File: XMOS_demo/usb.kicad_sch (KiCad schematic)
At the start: 9 parts, among them J2 USB_C_Receptacle_USB2.0_16P, U4 TPD3S014

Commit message: sch work
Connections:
- net P5V0: now also U4.4 (OUT)
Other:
- company: (none) -> AGH University
- title: (none) -> USB Sound Card USB Port
- moved on the sheet: C22, C25, FB2, R17, U4

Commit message: Lots of sch work
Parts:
- C22, C23, C25: Max Voltage 10V -> 16V
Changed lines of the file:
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@@
 			)
 		)
-		(property "Max Voltage" "10V"
+		(property "Max Voltage" "16V"
 			(at 180.34 81.28 0)
 			(effects
@@
 			)
 		)
-		(property "Max Voltage" "10V"
+		(property "Max Voltage" "16V"
 			(at 152.4 81.28 0)
 			(effects
@@
 			)
 		)
-		(property "Max Voltage" "10V"
+		(property "Max Voltage" "16V"
 			(at 170.18 81.28 0)
 			(effects

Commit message: sch work, pcb import and initial board outline
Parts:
- added H5: VBUS, MountingHole:MountingHole_5.3mm_M5_Pad_Via, symbol Mechanical:MountingHole_Pad
- added H6: GND, MountingHole:MountingHole_5.3mm_M5_Pad_Via, symbol Mechanical:MountingHole_Pad
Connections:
- net GND: now also H6.1
- net VBUS: now also H5.1
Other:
- moved on the sheet: J2

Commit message: terminal block for power input added
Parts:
- removed H5: VBUS, MountingHole:MountingHole_5.3mm_M5_Pad_Via, symbol Mechanical:MountingHole_Pad
- removed H6: GND, MountingHole:MountingHole_5.3mm_M5_Pad_Via, symbol Mechanical:MountingHole_Pad
- added J4: Screw_Terminal_P3.50mm, TerminalBlock_Phoenix:TerminalBlock_Phoenix_PT-1,5-2-3.5-H_1x02_P3.50mm_Horizontal, symbol Connector:Screw_Terminal_01x02
- added R45: 0R3, Resistor_SMD:R_0603_1608Metric, symbol Device:R_Small
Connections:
- net GND: now also R45.1
- net VBUS: now also J4.1 (Pin_1)
- new net: J4.2 (Pin_2), R45.2

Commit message: sch mostly finished, needs tp, pcb component layout started
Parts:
- removed C25: 100n, Capacitor_SMD:C_0603_1608Metric, symbol Device:C_Small
- removed R17: 43R, Resistor_SMD:R_0603_1608Metric, symbol Device:R_Small
- added J7: Conn_01x02_Pin, Connector_PinHeader_2.54mm:PinHeader_1x02_P2.54mm_Vertical, symbol Connector:Conn_01x02_Pin
- added R19: 0R, Resistor_SMD:R_0603_1608Metric, symbol Device:R_Small
- C22, C23: value 100n -> 1u
- J2: renamed from J4; value Screw_Terminal_P3.50mm -> Screw_Terminal
- renumbered J2 to J3, R45 to R18, R13 to R20, R14 to R21, U4 to U3
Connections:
- net GND: now also J7.2 (Pin_2)
- net VBUS: now also C22.1; no longer C23.1
- net VBUS_FILT: now reaches FB2.1, U3.3 (IN)
- net VBUS_FILT: now also C23.1, R19.1; no longer C22.1
- net at J2.2 (Pin_2), R18.2: now also J7.1 (Pin_1)
- net at U3.1 (EN): now also R19.2
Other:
- moved on the sheet: FB2, J2, R18, R20, R21, U3

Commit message: finished sch, pcb work
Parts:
- renumbered J7 to J3, J3 to J4, R18 to R16, R19 to R17, R20 to R18, R21 to R19
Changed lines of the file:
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@@
 		(on_board yes)
 		(dnp no)
-		(property "Reference" "#PWR031"
+		(property "Reference" "#PWR028"
 			(at 116.84 57.15 0)
 			(effects
@@
 			(project "XMOS_demo"
 				(path "/0a855fb0-ca19-4770-811e-70d8770d7fdd/0ad88a15-386f-4052-8899-c737373d7f63"
-					(reference "#PWR031")
+					(reference "#PWR028")
 					(unit 1)
 				)
@@
 		(on_board yes)
 		(dnp no)
-		(property "Reference" "R18"
+		(property "Reference" "R16"
 			(at 106.68 50.546 90)
 			(effects
@@
 			(project "XMOS_demo"
 				(path "/0a855fb0-ca19-4770-811e-70d8770d7fdd/0ad88a15-386f-4052-8899-c737373d7f63"
-					(reference "R18")
+					(reference "R16")
 					(unit 1)
 				)
@@
 		(on_board yes)
 		(dnp no)
-		(property "Reference" "R20"
+		(property "Reference" "R18"
 			(at 124.46 77.216 90)
 			(effects
@@
 			(project "XMOS_demo"
 				(path "/0a855fb0-ca19-4770-811e-70d8770d7fdd/0ad88a15-386f-4052-8899-c737373d7f63"
-					(reference "R20")
+					(reference "R18")
 					(unit 1)
 				)
@@
 		(on_board yes)
 		(dnp no)
-		(property "Reference" "#PWR038"
+		(property "Reference" "#PWR036"
 			(at 200.66 92.71 0)
 			(effects
@@
 			(project "XMOS_demo"
 				(path "/0a855fb0-ca19-4770-811e-70d8770d7fdd/0ad88a15-386f-4052-8899-c737373d7f63"
-					(reference "#PWR038")
+					(reference "#PWR036")
 					(unit 1)
 				)
@@
 		(on_board yes)
 		(dnp no)
-		(property "Reference" "J3"
+		(property "Reference" "J4"
 			(at 113.284 69.85 0)
 			(effects
@@
 			(project "XMOS_demo"
 				(path "/0a855fb0-ca19-4770-811e-70d8770d7fdd/0ad88a15-386f-4052-8899-c737373d7f63"
-					(reference "J3")
+					(reference "J4")
 					(unit 1)
 				)
@@
 		(on_board yes)
 		(dnp no)
-		(property "Reference" "#PWR030"
+		(property "Reference" "#PWR027"
 			(at 116.84 46.99 0)
 			(effects
@@
 			(project "XMOS_demo"
 				(path "/0a855fb0-ca19-4770-811e-70d8770d7fdd/0ad88a15-386f-4052-8899-c737373d7f63"
-					(reference "#PWR030")
+					(reference "#PWR027")
 					(unit 1)
 				)
@@
 		(on_board yes)
 		(dnp no)
-		(property "Reference" "#FLG01"
+		(property "Reference" "#FLG02"
 			(at 213.36 66.675 0)
 			(effects
@@
 			(project "XMOS_demo"
 				(path "/0a855fb0-ca19-4770-811e-70d8770d7fdd/0ad88a15-386f-4052-8899-c737373d7f63"
-					(reference "#FLG01")
+					(reference "#FLG02")
 					(unit 1)
 				)
@@
 		(on_board yes)
 		(dnp no)
-		(property "Reference" "#PWR095"
+		(property "Reference" "#PWR029"
 			(at 101.6 69.85 0)
 			(effects
@@
 			(project "XMOS_demo"
 				(path "/0a855fb0-ca19-4770-811e-70d8770d7fdd/0ad88a15-386f-4052-8899-c737373d7f63"
-					(reference "#PWR095")
+					(reference "#PWR029")
 					(unit 1)
 				)
@@
 		(on_board yes)
 		(dnp no)
-		(property "Reference" "#FLG02"
+		(property "Reference" "#FLG03"
 			(at 129.54 71.755 0)
 			(effects
@@
 			(project "XMOS_demo"
 				(path "/0a855fb0-ca19-4770-811e-70d8770d7fdd/0ad88a15-386f-4052-8899-c737373d7f63"
-					(reference "#FLG02")
+					(reference "#FLG03")
 					(unit 1)
 				)
@@
 		(on_board yes)
 		(dnp no)
-		(property "Reference" "#PWR032"
+		(property "Reference" "#PWR030"
 			(at 180.34 72.39 0)
 			(effects
@@
 			(project "XMOS_demo"
 				(path "/0a855fb0-ca19-4770-811e-70d8770d7fdd/0ad88a15-386f-4052-8899-c737373d7f63"
-					(reference "#PWR032")
+					(reference "#PWR030")
 					(unit 1)
 				)
@@
 		(on_board yes)
 		(dnp no)
-		(property "Reference" "#PWR033"
+		(property "Reference" "#PWR031"
 			(at 220.98 72.39 0)
 			(effects
@@
 			(project "XMOS_demo"
 				(path "/0a855fb0-ca19-4770-811e-70d8770d7fdd/0ad88a15-386f-4052-8899-c737373d7f63"
-					(reference "#PWR033")
+					(reference "#PWR031")
 					(unit 1)
 				)
@@
 		(on_board yes)
 		(dnp no)
-		(property "Reference" "#FLG03"
+		(property "Reference" "#FLG04"
 			(at 170.18 71.755 0)
 			(effects
@@
 			(project "XMOS_demo"
 				(path "/0a855fb0-ca19-4770-811e-70d8770d7fdd/0ad88a15-386f-4052-8899-c737373d7f63"
-					(reference "#FLG03")
+					(reference "#FLG04")
 					(unit 1)
 				)
@@
 		(on_board yes)
 		(dnp no)
-		(property "Reference" "#PWR035"
+		(property "Reference" "#PWR033"
 			(at 137.16 92.71 0)
 			(effects
@@
 			(project "XMOS_demo"
 				(path "/0a855fb0-ca19-4770-811e-70d8770d7fdd/0ad88a15-386f-4052-8899-c737373d7f63"
-					(reference "#PWR035")
+					(reference "#PWR033")
 					(unit 1)
 				)
@@
 		(on_board yes)
 		(dnp no)
-		(property "Reference" "#PWR034"
+		(property "Reference" "#PWR032"
 			(at 139.7 77.47 0)
 			(effects
@@
 			(project "XMOS_demo"
 				(path "/0a855fb0-ca19-4770-811e-70d8770d7fdd/0ad88a15-386f-4052-8899-c737373d7f63"
-					(reference "#PWR034")
+					(reference "#PWR032")
 					(unit 1)
 				)
@@
 		(on_board yes)
 		(dnp no)
-		(property "Reference" "R19"
+		(property "Reference" "R17"
 			(at 185.42 74.676 90)
 			(effects
@@
 			(project "XMOS_demo"
 				(path "/0a855fb0-ca19-4770-811e-70d8770d7fdd/0ad88a15-386f-4052-8899-c737373d7f63"
-					(reference "R19")
+					(reference "R17")
 					(unit 1)
 				)
@@
 		(on_board yes)
 		(dnp no)
-		(property "Reference" "#PWR039"
+		(property "Reference" "#PWR037"
 			(at 104.14 125.73 0)
 			(effects
@@
 			(project "XMOS_demo"
 				(path "/0a855fb0-ca19-4770-811e-70d8770d7fdd/0ad88a15-386f-4052-8899-c737373d7f63"
-					(reference "#PWR039")
+					(reference "#PWR037")
 					(unit 1)
 				)
@@
 		(on_board yes)
 		(dnp no)
-		(property "Reference" "R21"
+		(property "Reference" "R19"
 			(at 129.54 85.852 90)
 			(effects
@@
 			(project "XMOS_demo"
 				(path "/0a855fb0-ca19-4770-811e-70d8770d7fdd/0ad88a15-386f-4052-8899-c737373d7f63"
-					(reference "R21")
+					(reference "R19")
 					(unit 1)
 				)
@@
 		(on_board yes)
 		(dnp no)
-		(property "Reference" "#PWR037"
+		(property "Reference" "#PWR035"
 			(at 165.1 92.71 0)
 			(effects
@@
 			(project "XMOS_demo"
 				(path "/0a855fb0-ca19-4770-811e-70d8770d7fdd/0ad88a15-386f-4052-8899-c737373d7f63"
-					(reference "#PWR037")
+					(reference "#PWR035")
 					(unit 1)
 				)
@@
 		(on_board yes)
 		(dnp no)
-		(property "Reference" "J7"
+		(property "Reference" "J3"
 			(at 94.742 55.372 0)
 			(effects
@@
 			(project "XMOS_demo"
 				(path "/0a855fb0-ca19-4770-811e-70d8770d7fdd/0ad88a15-386f-4052-8899-c737373d7f63"
-					(reference "J7")
+					(reference "J3")
 					(unit 1)
 				)
@@
 		(on_board yes)
 		(dnp no)
-		(property "Reference" "#PWR036"
+		(property "Reference" "#PWR034"
 			(at 147.32 92.71 0)
 			(effects
@@
 			(project "XMOS_demo"
 				(path "/0a855fb0-ca19-4770-811e-70d8770d7fdd/0ad88a15-386f-4052-8899-c737373d7f63"
-					(reference "#PWR036")
-					(unit 1)
-				)
+					(reference "#PWR034")
+					(unit 1)
+				)

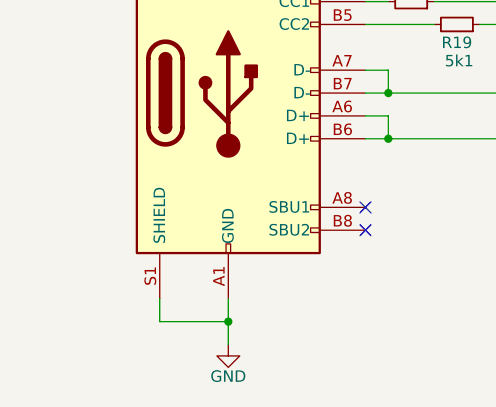
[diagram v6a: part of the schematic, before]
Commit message: PCB work, changes for better routing
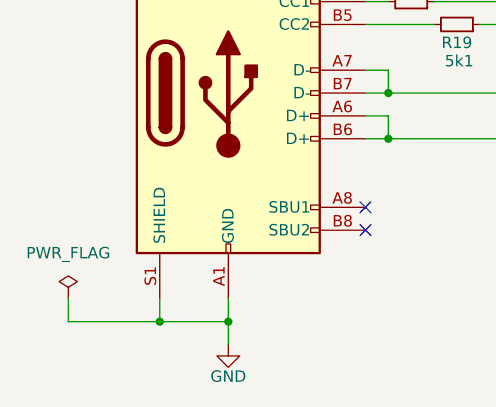
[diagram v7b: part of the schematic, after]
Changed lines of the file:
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@@
+	)
+	(junction
+		(at 96.52 116.84)
+		(diameter 0)
+		(color 0 0 0 0)
 	)
 	(junction
@@
 	(wire
 		(pts
+			(xy 86.36 116.84) (xy 96.52 116.84)
+		)
+		(stroke
+			(width 0)
+			(type default)
+		)
+	)
+	(wire
+		(pts
 			(xy 101.6 48.26) (xy 101.6 58.42)
 		)
@@
 		(pts
 			(xy 121.92 91.44) (xy 121.92 88.9)
+		)
+		(stroke
+			(width 0)
+			(type default)
+		)
+	)
+	(wire
+		(pts
+			(xy 86.36 114.3) (xy 86.36 116.84)
 		)
 		(stroke
@@
 					(unit 1)
 				)
+			)
+		)
+	)
+	(symbol
+		(lib_id "power:PWR_FLAG")
+		(at 86.36 114.3 0)
+		(unit 1)
+		(exclude_from_sim no)
+		(in_bom yes)
+		(on_board yes)
+		(dnp no)
+		(fields_autoplaced yes)
+		(property "Reference" "#FLG08"
+			(at 86.36 112.395 0)
+			(effects
+				(font
+					(size 1.27 1.27)
+				)
+				(hide yes)
+			)
+		)
+		(property "Value" "PWR_FLAG"
+			(at 86.36 109.22 0)
+			(effects
+				(font
+					(size 1.27 1.27)
+				)
+			)
+		)
+		(property "Footprint" ""
+			(at 86.36 114.3 0)
+			(effects
+				(font
+					(size 1.27 1.27)
+				)
+				(hide yes)
+			)
+		)
+		(property "Datasheet" "~"
+			(at 86.36 114.3 0)
+			(effects
+				(font
+					(size 1.27 1.27)
+				)
+				(hide yes)
+			)
+		)
+		(property "Description" "Special symbol for telling ERC where power comes from"
+			(at 86.36 114.3 0)
+			(effects
+				(font
+					(size 1.27 1.27)
+				)
+				(hide yes)
+			)
+		)
+		(pin "1"
+		)
+		(instances
+			(project "XMOS_demo"
+				(path "/0a855fb0-ca19-4770-811e-70d8770d7fdd/0ad88a15-386f-4052-8899-c737373d7f63"
+					(reference "#FLG08")
+					(unit 1)
+				)

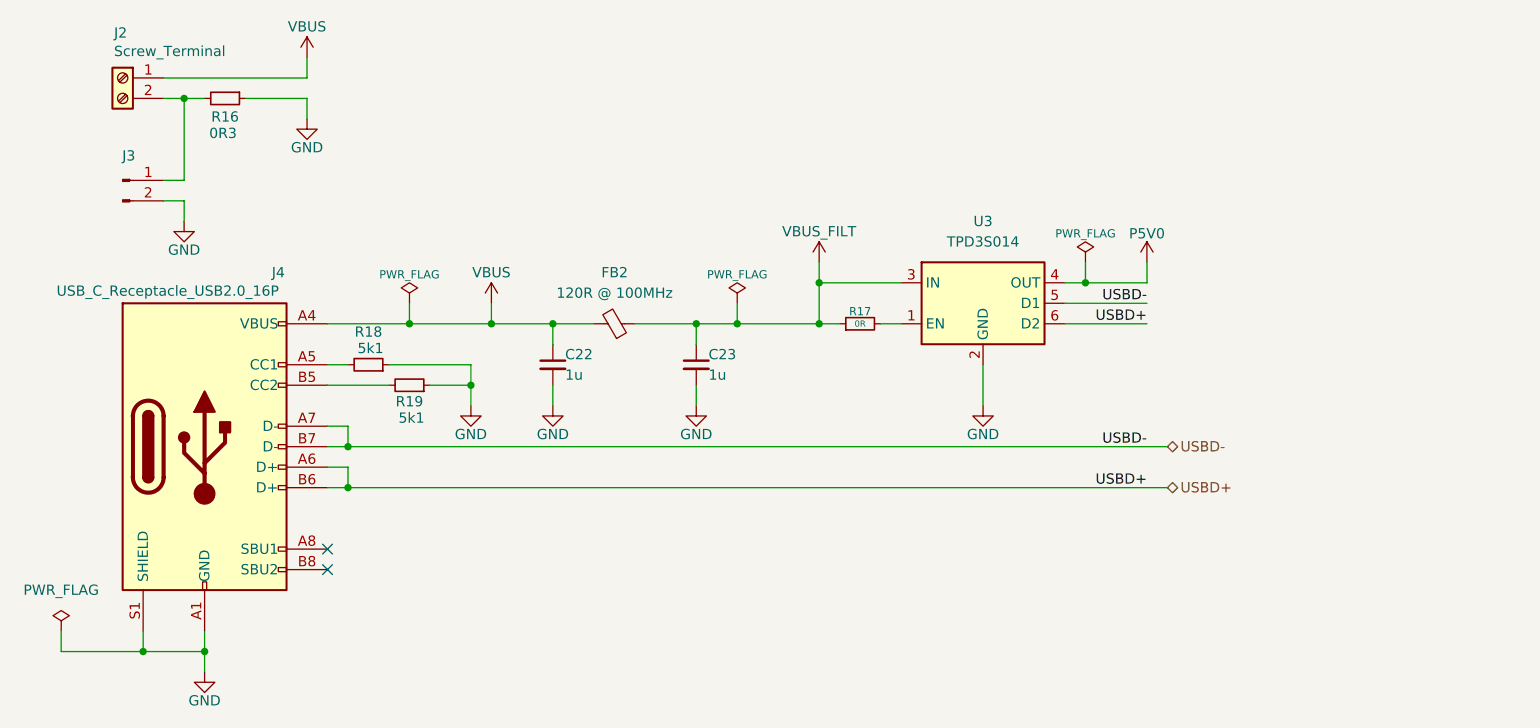
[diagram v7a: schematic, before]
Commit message: sch work changes (jumpers, connectors, tp)
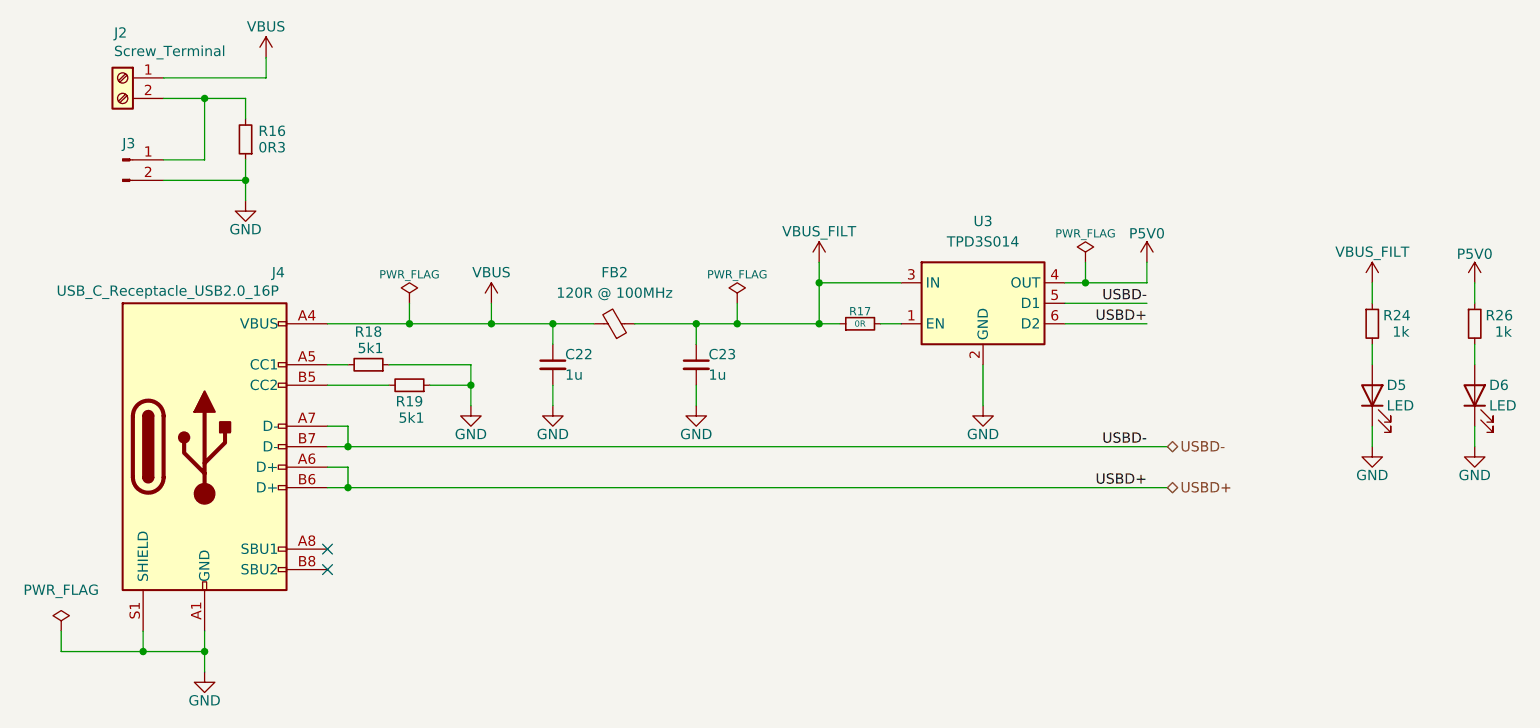
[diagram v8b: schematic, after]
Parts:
- added D5, D6: LED, LED_SMD:LED_0603_1608Metric, symbol Device:LED
- added R24, R26: 1k, Resistor_SMD:R_0603_1608Metric, symbol Device:R_Small
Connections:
- net GND: now also D5.1 (K), D6.1 (K)
- net P5V0: now also R26.1
- net VBUS_FILT: now also R24.1
- new net: D6.2 (A), R26.2
- new net: D5.2 (A), R24.2
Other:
- moved on the sheet: J3, R16
